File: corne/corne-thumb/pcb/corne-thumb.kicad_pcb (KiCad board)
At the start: 2 copper layers, 274.7 x 91.4 mm, 111 parts, among them J1 MJ-4PP-9, J2 OLED, J6 MJ-4PP-9, J7 OLED, SW1 SW_PUSH, SW10 SW_PUSH, SW11 SW_PUSH, SW12 SW_PUSH, SW13 SW_PUSH, SW14 SW_PUSH, SW15 SW_PUSH, SW16 SW_PUSH, SW17 SW_PUSH, SW18 SW_PUSH, SW19 SW_PUSH, SW2 SW_PUSH, SW20 SW_PUSH, SW21 SW_PUSH, SW22 SW_PUSH, SW23 SW_PUSH, SW24 SW_PUSH, SW25 SW_PUSH, SW26 SW_PUSH, SW27 SW_PUSH, SW28 SW_PUSH, SW29 SW_PUSH, SW3 SW_PUSH, SW30 SW_PUSH, SW31 SW_PUSH, SW32 SW_PUSH, SW33 SW_PUSH, SW34 SW_PUSH, SW35 SW_PUSH, SW36 SW_PUSH, SW37 SW_PUSH, SW38 SW_PUSH, SW39 SW_PUSH, SW4 SW_PUSH, SW41 SW_PUSH, SW42 SW_PUSH, SW5 SW_PUSH, SW6 SW_PUSH, SW7 SW_PUSH, SW8 SW_PUSH, SW9 SW_PUSH, U1 ProMicro, U2 ProMicro

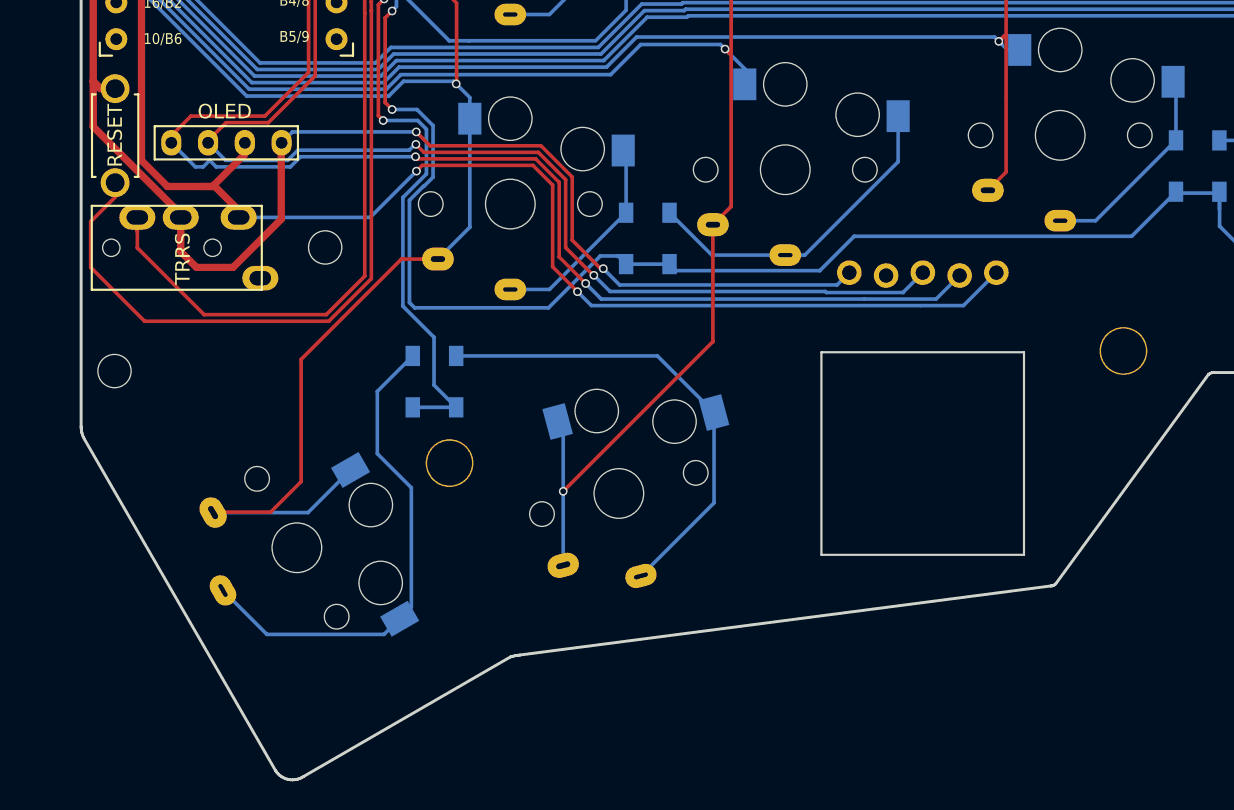
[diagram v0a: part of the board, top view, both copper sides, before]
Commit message: corne/thumb: move thumb trackball to the 42nd key position
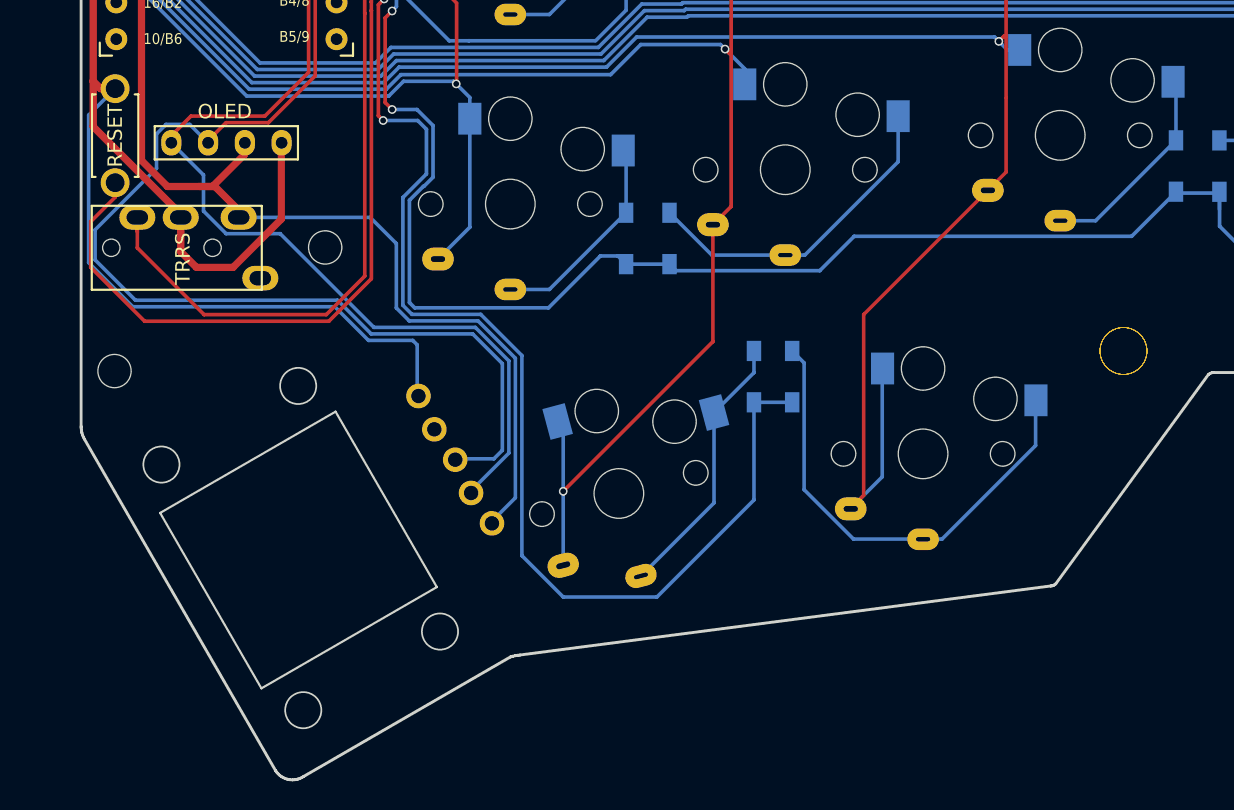
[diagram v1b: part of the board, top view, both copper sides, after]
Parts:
- removed D42: D, kbd:D3_SMD_v2
- removed the Ref** at (179.5, 99.4)
- removed SW42: SW_PUSH, keyswitches:Kailh_socket_PG1350_optional_oval_smaller_hotswap
- added D40: D, kbd:D3_SMD_v2, B.Cu at (203.2, 93.5)
- added Ref**: Val**, holykeebs:M2_SPACER, B.Cu at (226.1, 91.7)
- added Ref**: Val**, holykeebs:M2_SPACER, F.Cu at (226.1, 91.7)
- added SW40: SW_PUSH, keyswitches:Kailh_socket_PG1350_optional_oval_smaller_hotswap, F.Cu at (212.2, 98.8)
- moved U3 38.7 mm to (182.8, 103.4), turned to 120 degrees
- moved D41 20.6 mm to (200.5, 93.5)
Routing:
- net row3_r: track 40.7 -> 82.0 mm
- net col5_r: track 120.4 -> 81.8 mm
- net col3_r: track 129.9 -> 166.5 mm
- net Net-(D42-A): track 34.4 -> 0.00 mm
- net Net-(D40-A): track 0.00 -> 33.2 mm
- net VDD: track 105.2 -> 80.9 mm, vias 2 -> 0
- net SDA_r: track 96.3 -> 73.9 mm, vias 2 -> 0
- net Net-(D41-A): track 32.8 -> 18.8 mm
- net GNDA: track 124.9 -> 119.4 mm, vias 2 -> 0
- net SCL_r: track 85.8 -> 83.4 mm, vias 2 -> 0

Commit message: corne/thumb: bump version
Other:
- board text added: "9081e5e"

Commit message: corne thumb: update m2 spacer holes to be a tid bigger
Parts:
- removed the Ref** at (226.1, 91.7)
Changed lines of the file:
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@@
         (effects (font (size 1 1) (thickness 0.15)) (justify mirror))
     )
-    (fp_text user "${REFERENCE}" (at 3 -5) (layer "B.Fab")
+    (fp_text user "${VALUE}" (at 2.54 -0.635) (layer "B.Fab")
         (effects (font (size 1 1) (thickness 0.15)) (justify mirror))
     )
-    (fp_text user "${VALUE}" (at 2.54 -0.635) (layer "B.Fab")
+    (fp_text user "${REFERENCE}" (at 3 -5) (layer "B.Fab")
         (effects (font (size 1 1) (thickness 0.15)) (justify mirror))
     )
@@
     (fp_line (start 12.09 -6) (end -1.91 -6)
       (stroke (width 0.15) (type solid)) (layer "Edge.Cuts"))
-    (fp_circle (center -4.68 -7.35) (end -3.43 -7.35)
-      (stroke (width 0.12) (type solid)) (fill none) (layer "Edge.Cuts"))
     (fp_circle (center -4.66 -18.25) (end -3.41 -18.25)
       (stroke (width 0.12) (type solid)) (fill none) (layer "Edge.Cuts"))
-    (fp_circle (center 14.92 -7.35) (end 16.17 -7.35)
-      (stroke (width 0.12) (type solid)) (fill none) (layer "Edge.Cuts"))
     (fp_circle (center 14.94 -18.25) (end 16.19 -18.25)
       (stroke (width 0.12) (type solid)) (fill none) (layer "Edge.Cuts"))
@@
         (effects (font (size 1 1) (thickness 0.15)))
     )
-    (pad "" thru_hole circle (at 0 0) (size 3.3 3.3) (drill 3.1) (layers "*.Cu" "*.Mask")
-      (clearance 0.3))
+    (fp_circle (center 0 0) (end 2 0)
+      (stroke (width 0.1) (type default)) (fill none) (layer "Margin"))
+    (fp_circle (center 0 0) (end 2.25 0)
+      (stroke (width 0.1) (type default)) (fill none) (layer "Margin"))
+    (pad "" thru_hole circle (at 0 0) (size 3.5 3.5) (drill 3.3) (layers "*.Cu" "*.Mask"))
   )
   (footprint "holykeebs:M2_SPACER" (layer "F.Cu")
@@
         (effects (font (size 1 1) (thickness 0.15)))
     )
-    (pad "" thru_hole circle (at 0 0) (size 3.3 3.3) (drill 3.1) (layers "*.Cu" "*.Mask")
-      (clearance 0.3))
+    (fp_circle (center 0 0) (end 2 0)
+      (stroke (width 0.1) (type default)) (fill none) (layer "Margin"))
+    (fp_circle (center 0 0) (end 2.25 0)
+      (stroke (width 0.1) (type default)) (fill none) (layer "Margin"))
+    (pad "" thru_hole circle (at 0 0) (size 3.5 3.5) (drill 3.3) (layers "*.Cu" "*.Mask"))
   )
   (footprint "kbd:D3_SMD_v2" (layer "B.Cu")
@@
         (effects (font (size 1 1) (thickness 0.15)) (justify mirror))
     )
-    (pad "" thru_hole circle (at 0 0 180) (size 3.3 3.3) (drill 3.1) (layers "*.Cu" "*.Mask")
-      (clearance 0.3))
+    (fp_circle (center 0 0) (end 2 0)
+      (stroke (width 0.1) (type default)) (fill none) (layer "Margin"))
+    (fp_circle (center 0 0) (end 2.25 0)
+      (stroke (width 0.1) (type default)) (fill none) (layer "Margin"))
+    (pad "" thru_hole circle (at 0 0 180) (size 3.5 3.5) (drill 3.3) (layers "*.Cu" "*.Mask"))
   )
   (footprint "holykeebs:M2_SPACER" (layer "B.Cu")
@@
         (effects (font (size 1 1) (thickness 0.15)) (justify mirror))
     )
-    (pad "" thru_hole circle (at 0 0 180) (size 3.3 3.3) (drill 3.1) (layers "*.Cu" "*.Mask")
-      (clearance 0.3))
+    (fp_circle (center 0 0) (end 2 0)
+      (stroke (width 0.1) (type default)) (fill none) (layer "Margin"))
+    (fp_circle (center 0 0) (end 2.25 0)
+      (stroke (width 0.1) (type default)) (fill none) (layer "Margin"))
+    (pad "" thru_hole circle (at 0 0 180) (size 3.5 3.5) (drill 3.3) (layers "*.Cu" "*.Mask"))
   )
   (footprint "holykeebs:M2_SPACER" (layer "B.Cu")
@@
         (effects (font (size 1 1) (thickness 0.15)) (justify mirror))
     )
-    (pad "" thru_hole circle (at 0 0 180) (size 3.3 3.3) (drill 3.1) (layers "*.Cu" "*.Mask")
-      (clearance 0.3))
+    (fp_circle (center 0 0) (end 2 0)
+      (stroke (width 0.1) (type default)) (fill none) (layer "Margin"))
+    (fp_circle (center 0 0) (end 2.25 0)
+      (stroke (width 0.1) (type default)) (fill none) (layer "Margin"))
+    (pad "" thru_hole circle (at 0 0 180) (size 3.5 3.5) (drill 3.3) (layers "*.Cu" "*.Mask"))
   )
   (footprint "holykeebs:M2_SPACER" (layer "B.Cu")
@@
         (effects (font (size 1 1) (thickness 0.15)) (justify mirror))
     )
-    (pad "" thru_hole circle (at 0 0 180) (size 3.3 3.3) (drill 3.1) (layers "*.Cu" "*.Mask")
-      (clearance 0.3))
+    (fp_circle (center 0 0) (end 2 0)
+      (stroke (width 0.1) (type default)) (fill none) (layer "Margin"))
+    (fp_circle (center 0 0) (end 2.25 0)
+      (stroke (width 0.1) (type default)) (fill none) (layer "Margin"))
+    (pad "" thru_hole circle (at 0 0 180) (size 3.5 3.5) (drill 3.3) (layers "*.Cu" "*.Mask"))
   )
   (footprint "holykeebs:M2_SPACER" (layer "B.Cu")
@@
         (effects (font (size 1 1) (thickness 0.15)) (justify mirror))
     )
-    (pad "" thru_hole circle (at 0 0 180) (size 3.3 3.3) (drill 3.1) (layers "*.Cu" "*.Mask")
-      (clearance 0.3))
+    (fp_circle (center 0 0) (end 2 0)
+      (stroke (width 0.1) (type default)) (fill none) (layer "Margin"))
+    (fp_circle (center 0 0) (end 2.25 0)
+      (stroke (width 0.1) (type default)) (fill none) (layer "Margin"))
+    (pad "" thru_hole circle (at 0 0 180) (size 3.5 3.5) (drill 3.3) (layers "*.Cu" "*.Mask"))
   )
   (footprint "kbd:thread_m2" (layer "B.Cu")
@@
         (effects (font (size 1 1) (thickness 0.15)) (justify mirror))
     )
-    (pad "" thru_hole circle (at 0 0 180) (size 3.3 3.3) (drill 3.1) (layers "*.Cu" "*.Mask")
-      (clearance 0.3))
-  )
-  (footprint "holykeebs:M2_SPACER" (layer "B.Cu")
-    (at 226.055847 91.696932 180)
-    (attr through_hole)
-    (fp_text reference "Ref**" (at 0 0.5 unlocked) (layer "B.SilkS") hide
-        (effects (font (size 1 1) (thickness 0.1)) (justify mirror))
-    )
-    (fp_text value "Val**" (at 0 -1 unlocked) (layer "B.Fab") hide
-        (effects (font (size 1 1) (thickness 0.15)) (justify mirror))
-    )
-    (fp_text user "${REFERENCE}" (at 0.3 0) (layer "B.Fab")
-        (effects (font (size 1 1) (thickness 0.15)) (justify mirror))
-    )
-    (pad "" thru_hole circle (at 0 0 180) (size 3.3 3.3) (drill 3.1) (layers "*.Cu" "*.Mask")
-      (clearance 0.3))
+    (fp_circle (center 0 0) (end 2 0)
+      (stroke (width 0.1) (type default)) (fill none) (layer "Margin"))
+    (fp_circle (center 0 0) (end 2.25 0)
+      (stroke (width 0.1) (type default)) (fill none) (layer "Margin"))
+    (pad "" thru_hole circle (at 0 0 180) (size 3.5 3.5) (drill 3.3) (layers "*.Cu" "*.Mask"))
   )
   (footprint "holykeebs:M2_SPACER" (layer "B.Cu")
@@
         (effects (font (size 1 1) (thickness 0.15)) (justify mirror))
     )
-    (pad "" thru_hole circle (at 0 0 180) (size 3.3 3.3) (drill 3.1) (layers "*.Cu" "*.Mask")
-      (clearance 0.3))
+    (fp_circle (center 0 0) (end 2 0)
+      (stroke (width 0.1) (type default)) (fill none) (layer "Margin"))
+    (fp_circle (center 0 0) (end 2.25 0)
+      (stroke (width 0.1) (type default)) (fill none) (layer "Margin"))
+    (pad "" thru_hole circle (at 0 0 180) (size 3.5 3.5) (drill 3.3) (layers "*.Cu" "*.Mask"))
   )
   (footprint "kbd:corne-logo-horizontal" (layer "B.Cu")
@@
         (effects (font (size 1 1) (thickness 0.15)) (justify mirror))
     )
-    (pad "" thru_hole circle (at 0 0 180) (size 3.3 3.3) (drill 3.1) (layers "*.Cu" "*.Mask")
-      (clearance 0.3))
+    (fp_circle (center 0 0) (end 2 0)
+      (stroke (width 0.1) (type default)) (fill none) (layer "Margin"))
+    (fp_circle (center 0 0) (end 2.25 0)
+      (stroke (width 0.1) (type default)) (fill none) (layer "Margin"))
+    (pad "" thru_hole circle (at 0 0 180) (size 3.5 3.5) (drill 3.3) (layers "*.Cu" "*.Mask"))
   )
   (gr_line (start 146.633773 37.028537) (end 146.501693 36.959958)

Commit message: corne/thumb: bump version
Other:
- board text added: "9246575"
- board text removed: "9081e5e"
